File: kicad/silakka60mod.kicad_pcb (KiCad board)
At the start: 4 copper layers, 313 x 114.1 mm, 124 parts, among them J1 AudioJack4, J2 AudioJack4, U1 RP2040_Zero, U2 RP2040_Zero

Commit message: Add files via upload
done some cleanup on traces and moved all vias from pads
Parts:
- added REF**: KiCad-Logo_5mm_SilkScreen, Symbol:KiCad-Logo_5mm_SilkScreen, F.Cu at (124.2, 85.6)
- added REF**: KiCad-Logo_5mm_SilkScreen, Symbol:KiCad-Logo_5mm_SilkScreen, F.Cu at (171.8, 84.9)
- added REF**: OSHW-Logo_11.4x12mm_SilkScreen, Symbol:OSHW-Logo_11.4x12mm_SilkScreen, F.Cu at (172.3, 70.5)
- added REF**: OSHW-Logo_11.4x12mm_SilkScreen, Symbol:OSHW-Logo_11.4x12mm_SilkScreen, F.Cu at (123.8, 71.2)
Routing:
- net ROW3: track 226.3 -> 215.4 mm
- net ROW2: track 197.0 -> 186.9 mm
- net COL0: track 224.3 -> 232.6 mm
- net COL0b: track 233.1 -> 240.0 mm
- net COL5b: track 160.3 -> 166.5 mm
- net COL1b: track 214.6 -> 220.5 mm
- net COL3b: track 186.9 -> 192.7 mm
- net Net-(D26-A): track 13.8 -> 19.4 mm, vias 1 -> 0
- net Net-(D25-A): track 13.9 -> 19.4 mm, vias 1 -> 0
- net COL4b: track 172.6 -> 178.1 mm
- net Net-(D27-A): track 13.9 -> 19.3 mm, vias 1 -> 0
- net ROW0: track 160.6 -> 155.2 mm
- net Net-(D28-A): track 13.9 -> 19.1 mm, vias 1 -> 0
- net Net-(D24-A): track 13.9 -> 18.9 mm
- net Net-(D30-A): track 29.2 -> 33.8 mm
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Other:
- copper layers 4 -> 2

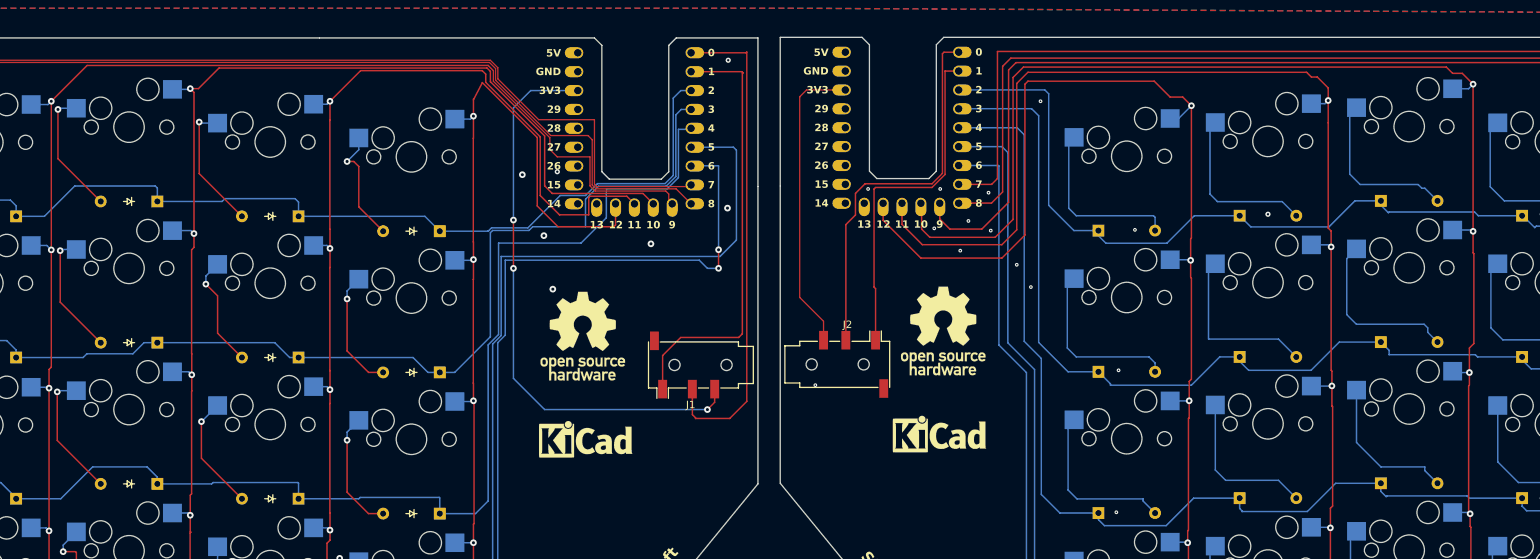
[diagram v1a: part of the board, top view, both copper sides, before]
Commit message: Add files via upload
more minor fixes and I started adding mounting holes
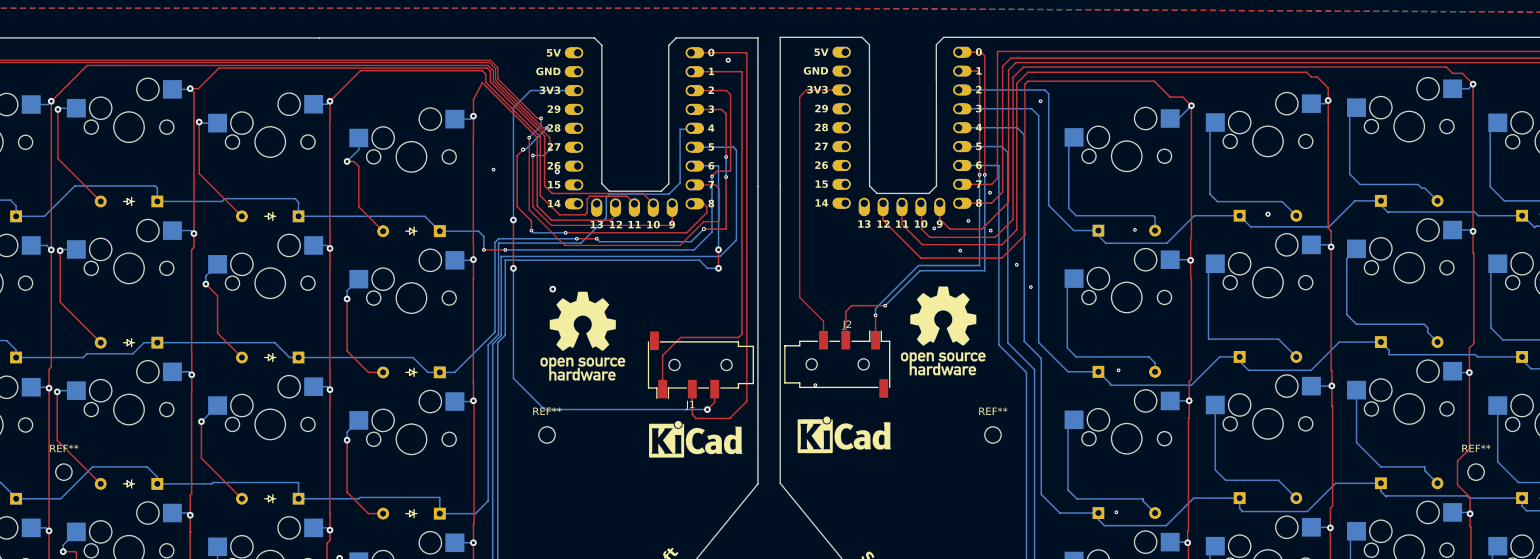
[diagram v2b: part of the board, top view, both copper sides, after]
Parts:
- added REF**: MountingHole_2.2mm_M2, MountingHole:MountingHole_2.2mm_M2, F.Cu at (54.0, 89.5)
- added REF**: MountingHole_2.2mm_M2, MountingHole:MountingHole_2.2mm_M2, F.Cu at (244.0, 89.5)
- added REF**: MountingHole_2.2mm_M2, MountingHole:MountingHole_2.2mm_M2, F.Cu at (179.0, 84.5)
- added REF**: MountingHole_2.2mm_M2, MountingHole:MountingHole_2.2mm_M2, F.Cu at (119.0, 84.5)
- moved REF** 14.8 mm to (139.0, 85.6)
- moved REF** 12.8 mm to (159.0, 85.0)
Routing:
- net COL0: track 232.6 -> 254.1 mm, vias 5 -> 7
- net ROW0: track 155.2 -> 173.3 mm, vias 0 -> 3
- net COL1: track 210.4 -> 227.6 mm, vias 5 -> 10
- net ROW1: track 166.1 -> 176.8 mm, vias 0 -> 6
- net COL2: track 189.3 -> 199.8 mm, vias 5 -> 7
- net TXb: track 51.5 -> 57.5 mm, vias 0 -> 2
- net RXb: track 46.5 -> 49.4 mm, vias 0 -> 2
- net COL5: track 134.1 -> 132.6 mm
- net COL3b: track 192.7 -> 193.9 mm
- net GND: vias 26 -> 21
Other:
- outline, holes or cut-outs redrawn

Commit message: Production!
production of a first batch started! is boards will end up working i will start working on firmware side. Another thing to learn!
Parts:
- moved REF** 0.30 mm to (54.0, 89.8)
- moved REF** 0.30 mm to (244.0, 89.8)
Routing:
- net COL3: track 168.6 -> 172.1 mm, vias 5 -> 7
- net ROW2: track 186.7 -> 189.7 mm
- net COL1: track 227.6 -> 230.1 mm
- net COL4: track 148.6 -> 149.9 mm
